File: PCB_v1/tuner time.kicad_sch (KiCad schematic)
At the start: 13 parts, among them U1 C1F 2

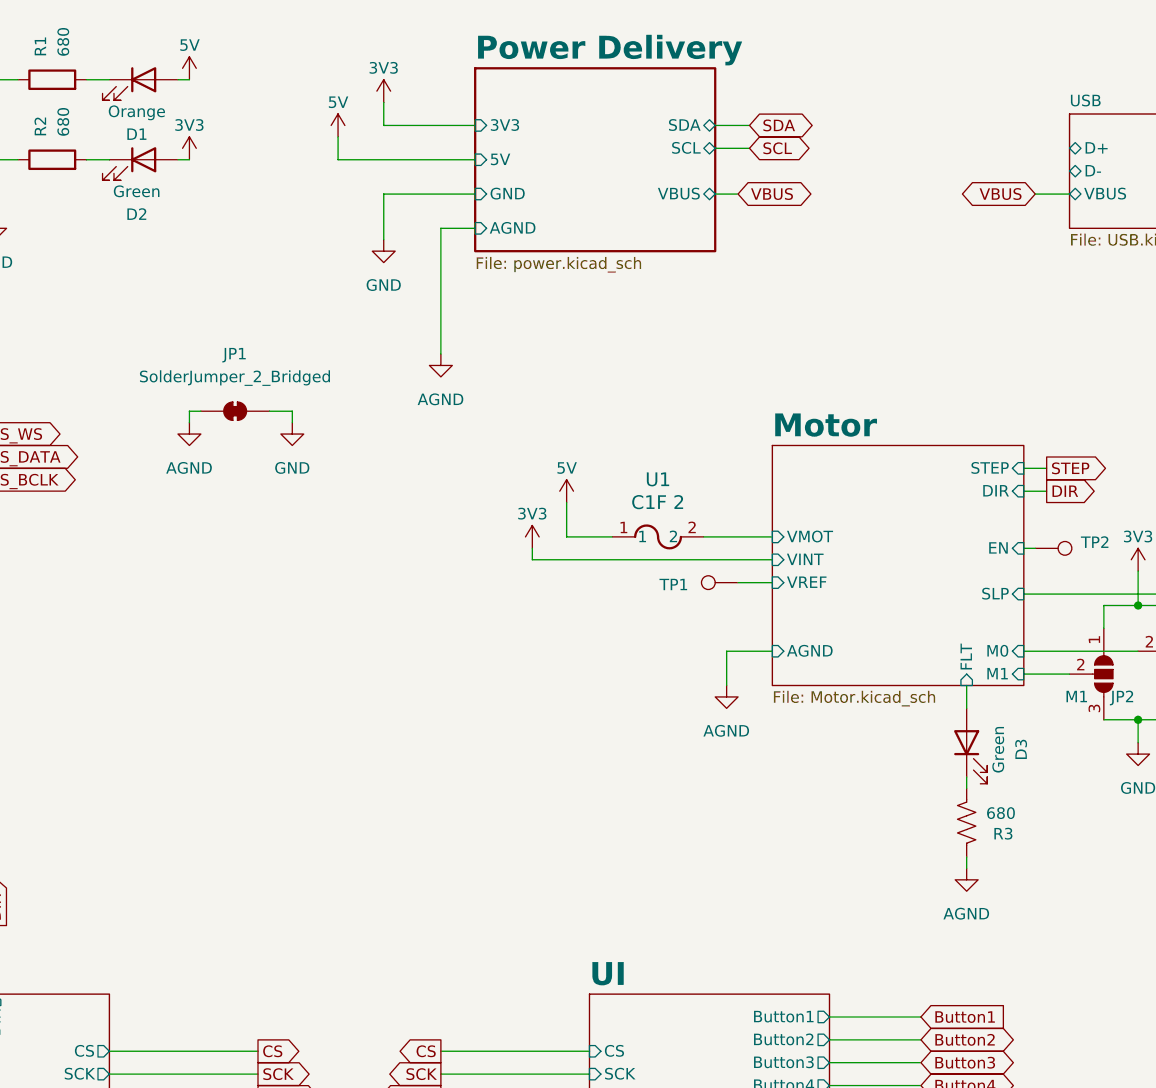
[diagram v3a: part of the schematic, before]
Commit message: Main routes done, no power planes, no DRC
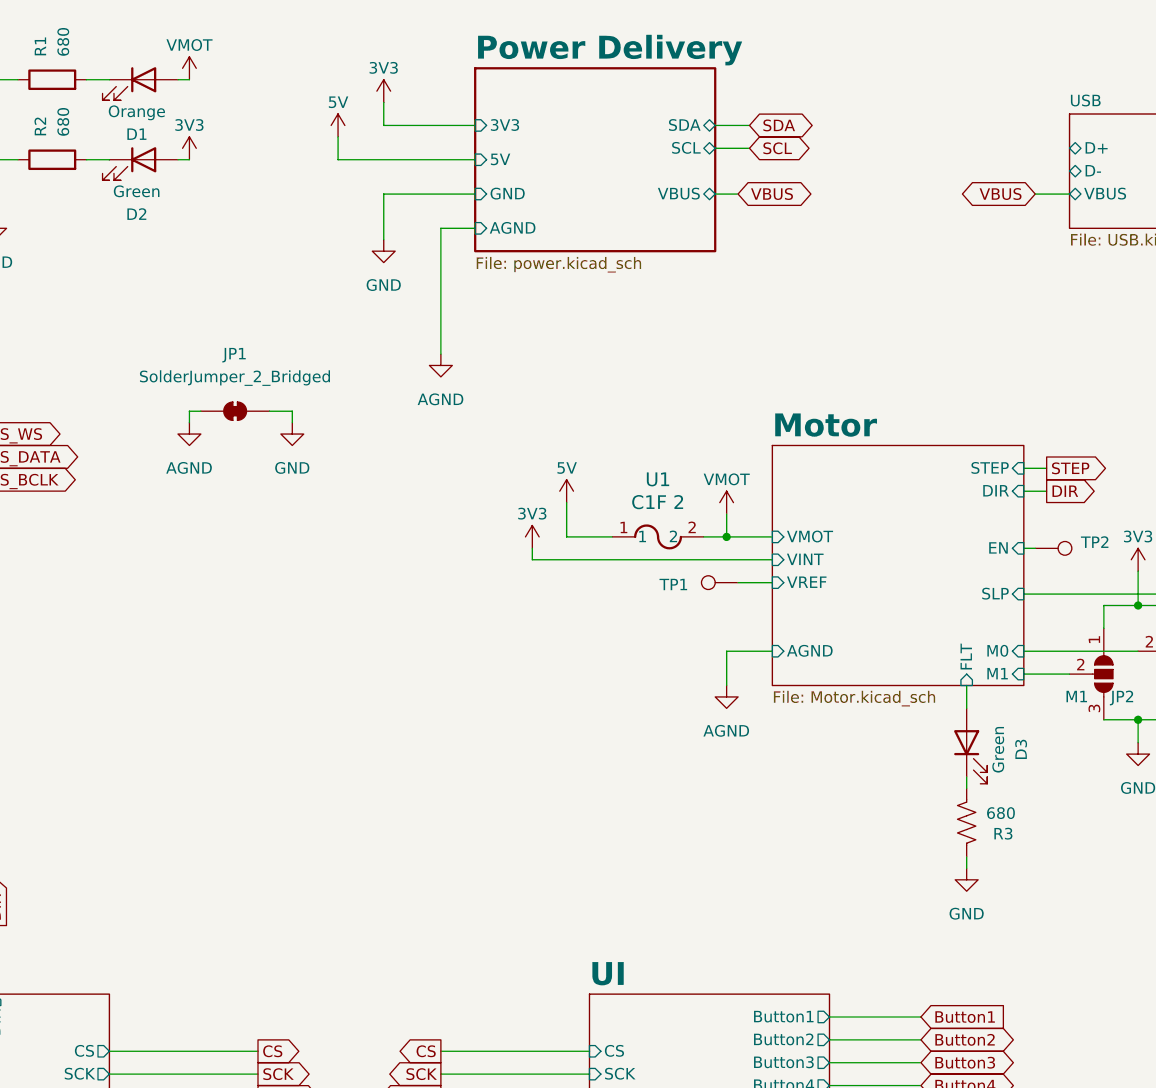
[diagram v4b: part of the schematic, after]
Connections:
- net 5V: no longer D1.2 (A)
- net AGND: no longer R3.2
- net GND: now also R3.2
- net Motor/VMOT renamed VMOT
- net VMOT: now also D1.2 (A)
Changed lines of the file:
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@@
 		(color 0 0 0 0)
 	)
+	(junction
+		(at 198.12 74.93)
+		(diameter 0)
+		(color 0 0 0 0)
+	)
 	(wire
 		(pts
@@
 	(wire
 		(pts
+			(xy 198.12 72.39) (xy 198.12 74.93)
+		)
+		(stroke
+			(width 0)
+			(type default)
+		)
+	)
+	(wire
+		(pts
 			(xy 149.86 60.96) (xy 147.32 60.96)
 		)
@@
 	(wire
 		(pts
+			(xy 198.12 74.93) (xy 203.2 74.93)
+		)
+		(stroke
+			(width 0)
+			(type default)
+		)
+	)
+	(wire
+		(pts
 			(xy 232.41 36.83) (xy 236.22 36.83)
 		)
@@
 	(wire
 		(pts
-			(xy 195.58 74.93) (xy 203.2 74.93)
+			(xy 195.58 74.93) (xy 198.12 74.93)
 		)
 		(stroke
@@
 			)
 		)
-		(property "Value" "AGND"
+		(property "Value" "GND"
 			(at 224.79 116.84 0)
 			(effects
@@
 	)
 	(symbol
-		(lib_id "power:VCC")
-		(at 138.43 24.13 0)
-		(unit 1)
-		(exclude_from_sim no)
-		(in_bom yes)
-		(on_board yes)
-		(dnp no)
-		(property "Reference" "#PWR07"
-			(at 138.43 27.94 0)
-			(effects
-				(font
-					(size 1.27 1.27)
-				)
-				(hide yes)
-			)
-		)
-		(property "Value" "5V"
-			(at 138.43 20.32 0)
-			(effects
-				(font
-					(size 1.27 1.27)
-				)
-			)
-		)
-		(property "Footprint" ""
-			(at 138.43 24.13 0)
-			(effects
-				(font
-					(size 1.27 1.27)
-				)
-				(hide yes)
-			)
-		)
-		(property "Datasheet" ""
-			(at 138.43 24.13 0)
-			(effects
-				(font
-					(size 1.27 1.27)
-				)
-				(hide yes)
-			)
-		)
-		(property "Description" "Power symbol creates a global label with name \"VCC\""
-			(at 138.43 24.13 0)
-			(effects
-				(font
-					(size 1.27 1.27)
-				)
-				(hide yes)
-			)
-		)
-		(pin "1"
-		)
-		(instances
-			(project "tuner time"
-				(path "/353cef6a-fb6e-40d9-89f8-eb54b7aa5118"
-					(reference "#PWR07")
-					(unit 1)
-				)
-			)
-		)
-	)
-	(symbol
 		(lib_id "power:GND")
 		(at 116.84 39.37 0)
@@
 	)
 	(symbol
+		(lib_id "power:VCC")
+		(at 138.43 24.13 0)
+		(unit 1)
+		(exclude_from_sim no)
+		(in_bom yes)
+		(on_board yes)
+		(dnp no)
+		(property "Reference" "#PWR0115"
+			(at 138.43 27.94 0)
+			(effects
+				(font
+					(size 1.27 1.27)
+				)
+				(hide yes)
+			)
+		)
+		(property "Value" "VMOT"
+			(at 138.43 20.32 0)
+			(effects
+				(font
+					(size 1.27 1.27)
+				)
+			)
+		)
+		(property "Footprint" ""
+			(at 138.43 24.13 0)
+			(effects
+				(font
+					(size 1.27 1.27)
+				)
+				(hide yes)
+			)
+		)
+		(property "Datasheet" ""
+			(at 138.43 24.13 0)
+			(effects
+				(font
+					(size 1.27 1.27)
+				)
+				(hide yes)
+			)
+		)
+		(property "Description" "Power symbol creates a global label with name \"VCC\""
+			(at 138.43 24.13 0)
+			(effects
+				(font
+					(size 1.27 1.27)
+				)
+				(hide yes)
+			)
+		)
+		(pin "1"
+		)
+		(instances
+			(project "tuner time"
+				(path "/353cef6a-fb6e-40d9-89f8-eb54b7aa5118"
+					(reference "#PWR0115")
+					(unit 1)
+				)
+			)
+		)
+	)
+	(symbol
 		(lib_id "power:GND")
 		(at 166.37 54.61 0)
@@
 					(unit 1)
 				)
+			)
+		)
+	)
+	(symbol
+		(lib_id "power:VCC")
+		(at 198.12 72.39 0)
+		(unit 1)
+		(exclude_from_sim no)
+		(in_bom yes)
+		(on_board yes)
+		(dnp no)
+		(property "Reference" "#PWR07"
+			(at 198.12 76.2 0)
+			(effects
+				(font
+					(size 1.27 1.27)
+				)
+				(hide yes)
+			)
+		)
+		(property "Value" "VMOT"
+			(at 198.12 68.58 0)
+			(effects
+				(font
+					(size 1.27 1.27)
+				)
+			)
+		)
+		(property "Footprint" ""
+			(at 198.12 72.39 0)
+			(effects
+				(font
+					(size 1.27 1.27)
+				)
+				(hide yes)
+			)
+		)
+		(property "Datasheet" ""
+			(at 198.12 72.39 0)
+			(effects
+				(font
+					(size 1.27 1.27)
+				)
+				(hide yes)
+			)
+		)
+		(property "Description" "Power symbol creates a global label with name \"VCC\""
+			(at 198.12 72.39 0)
+			(effects
+				(font
+					(size 1.27 1.27)
+				)
+				(hide yes)
+			)
+		)
+		(pin "1"
+		)
+		(instances
+			(project "tuner time"
+				(path "/353cef6a-fb6e-40d9-89f8-eb54b7aa5118"
+					(reference "#PWR07")
+					(unit 1)
+				)

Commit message: Power Layout done
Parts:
- added H1, H2: MountingHole, MountingHole:MountingHole_2.2mm_M2_DIN965_Pad_TopOnly, symbol Mechanical:MountingHole
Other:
- sheet MCU ports: added BAT_EMPTY; removed none
- sheet Power Delivery ports: added BAT_EMPTY; removed none
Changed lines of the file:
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@@
 	(wire
 		(pts
+			(xy 199.39 40.64) (xy 196.85 40.64)
+		)
+		(stroke
+			(width 0)
+			(type default)
+		)
+	)
+	(wire
+		(pts
 			(xy 243.84 78.74) (xy 243.84 82.55)
 		)
@@
 	(wire
 		(pts
+			(xy 129.54 152.4) (xy 139.7 152.4)
+		)
+		(stroke
+			(width 0)
+			(type default)
+		)
+	)
+	(wire
+		(pts
 			(xy 209.55 138.43) (xy 219.71 138.43)
 		)
@@
 		)
 	)
+	(global_label "BAT_EMPTY"
+		(shape input)
+		(at 139.7 152.4 0)
+		(fields_autoplaced yes)
+		(effects
+			(font
+				(size 1.27 1.27)
+			)
+			(justify left)
+		)
+		(property "Intersheetrefs" "${INTERSHEET_REFS}"
+			(at 152.9056 152.4 0)
+			(effects
+				(font
+					(size 1.27 1.27)
+				)
+				(justify left)
+				(hide yes)
+			)
+		)
+	)
 	(global_label "SCK"
 		(shape output)
@@
 		)
 	)
+	(global_label "BAT_EMPTY"
+		(shape input)
+		(at 199.39 40.64 0)
+		(fields_autoplaced yes)
+		(effects
+			(font
+				(size 1.27 1.27)
+			)
+			(justify left)
+		)
+		(property "Intersheetrefs" "${INTERSHEET_REFS}"
+			(at 212.5956 40.64 0)
+			(effects
+				(font
+					(size 1.27 1.27)
+				)
+				(justify left)
+				(hide yes)
+			)
+		)
+	)
 	(global_label "MOSI"
 		(shape output)
@@
 	)
 	(symbol
+		(lib_id "Mechanical:MountingHole")
+		(at 19.05 17.78 0)
+		(unit 1)
+		(exclude_from_sim yes)
+		(in_bom no)
+		(on_board yes)
+		(dnp no)
+		(fields_autoplaced yes)
+		(property "Reference" "H1"
+			(at 21.59 16.5099 0)
+			(effects
+				(font
+					(size 1.27 1.27)
+				)
+				(justify left)
+			)
+		)
+		(property "Value" "MountingHole"
+			(at 21.59 19.0499 0)
+			(effects
+				(font
+					(size 1.27 1.27)
+				)
+				(justify left)
+			)
+		)
+		(property "Footprint" "MountingHole:MountingHole_2.2mm_M2_DIN965_Pad_TopOnly"
+			(at 19.05 17.78 0)
+			(effects
+				(font
+					(size 1.27 1.27)
+				)
+				(hide yes)
+			)
+		)
+		(property "Datasheet" "~"
+			(at 19.05 17.78 0)
+			(effects
+				(font
+					(size 1.27 1.27)
+				)
+				(hide yes)
+			)
+		)
+		(property "Description" "Mounting Hole without connection"
+			(at 19.05 17.78 0)
+			(effects
+				(font
+					(size 1.27 1.27)
+				)
+				(hide yes)
+			)
+		)
+		(instances
+			(project ""
+				(path "/353cef6a-fb6e-40d9-89f8-eb54b7aa5118"
+					(reference "H1")
+					(unit 1)
+				)
+			)
+		)
+	)
+	(symbol
 		(lib_id "power:VCC")
 		(at 180.34 71.12 0)
@@
 	)
 	(symbol
+		(lib_id "Mechanical:MountingHole")
+		(at 19.05 24.13 0)
+		(unit 1)
+		(exclude_from_sim yes)
+		(in_bom no)
+		(on_board yes)
+		(dnp no)
+		(fields_autoplaced yes)
+		(property "Reference" "H2"
+			(at 21.59 22.8599 0)
+			(effects
+				(font
+					(size 1.27 1.27)
+				)
+				(justify left)
+			)
+		)
+		(property "Value" "MountingHole"
+			(at 21.59 25.3999 0)
+			(effects
+				(font
+					(size 1.27 1.27)
+				)
+				(justify left)
+			)
+		)
+		(property "Footprint" "MountingHole:MountingHole_2.2mm_M2_DIN965_Pad_TopOnly"
+			(at 19.05 24.13 0)
+			(effects
+				(font
+					(size 1.27 1.27)
+				)
+				(hide yes)
+			)
+		)
+		(property "Datasheet" "~"
+			(at 19.05 24.13 0)
+			(effects
+				(font
+					(size 1.27 1.27)
+				)
+				(hide yes)
+			)
+		)
+		(property "Description" "Mounting Hole without connection"
+			(at 19.05 24.13 0)
+			(effects
+				(font
+					(size 1.27 1.27)
+				)
+				(hide yes)
+			)
+		)
+		(instances
+			(project "tuner time"
+				(path "/353cef6a-fb6e-40d9-89f8-eb54b7aa5118"
+					(reference "H2")
+					(unit 1)
+				)
+			)
+		)
+	)
+	(symbol
 		(lib_id "power:GND")
 		(at 254 87.63 0)
@@
 			)
 		)
+		(pin "BAT_EMPTY" output
+			(at 196.85 40.64 0)
+			(effects
+				(font
+					(size 1.27 1.27)
+				)
+				(justify right)
+			)
+		)
 		(instances
 			(project "tuner time"
@@
 			)
 		)
+		(pin "BAT_EMPTY" input
+			(at 129.54 152.4 0)
+			(effects
+				(font
+					(size 1.27 1.27)
+				)
+				(justify right)
+			)
+		)

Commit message: before annonation reset
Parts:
- F2: renamed from U1; MFP (none) -> 5923-C1F2TR-ND
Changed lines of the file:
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@@
 		(dnp no)
 		(fields_autoplaced yes)
-		(property "Reference" "U1"
+		(property "Reference" "F2"
 			(at 190.5 68.58 0)
 			(effects
@@
 			)
 		)
-		(property "MFP" ""
+		(property "MFP" "5923-C1F2TR-ND"
 			(at 185.42 74.93 0)
 			(effects
@@
 			(project ""
 				(path "/353cef6a-fb6e-40d9-89f8-eb54b7aa5118"
-					(reference "U1")
+					(reference "F2")
 					(unit 1)
 				)

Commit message: pushing BOM
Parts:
- F1: renamed from F2; MFP 5923-C1F2TR-ND -> C1F 2 (CA0612KRX7R7BB104)
- H1, H2, JP1, JP2, JP3, JP4, TP1, TP2: MFP (none) -> N/A
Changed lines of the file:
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@@
 		(dnp no)
 		(fields_autoplaced yes)
-		(property "Reference" "F2"
+		(property "Reference" "F1"
 			(at 190.5 68.58 0)
 			(effects
@@
 			)
 		)
-		(property "Datasheet" "C1F 2"
+		(property "Datasheet" ""
 			(at 185.42 74.93 0)
 			(effects
@@
 			)
 		)
-		(property "MFP" "5923-C1F2TR-ND"
+		(property "MFP" "C1F 2 (CA0612KRX7R7BB104)"
 			(at 185.42 74.93 0)
 			(effects
@@
 			(project ""
 				(path "/353cef6a-fb6e-40d9-89f8-eb54b7aa5118"
-					(reference "F2")
+					(reference "F1")
 					(unit 1)
 				)
@@
 			)
 		)
+		(property "MFP" "N/A"
+			(at 143.51 60.96 0)
+			(effects
+				(font
+					(size 1.27 1.27)
+				)
+				(hide yes)
+			)
+		)
 		(pin "2"
 		)
@@
 			)
 		)
-		(property "MFP" ""
+		(property "MFP" "N/A"
 			(at 232.41 76.2 0)
 			(effects
@@
 			)
 		)
-		(property "MFP" ""
+		(property "MFP" "N/A "
 			(at 240.03 90.17 0)
 			(effects
@@
 		(dnp no)
 		(fields_autoplaced yes)
-		(property "Reference" "#PWR020"
+		(property "Reference" "#PWR021"
 			(at 224.79 118.11 0)
 			(effects
@@
 			(project "tuner time"
 				(path "/353cef6a-fb6e-40d9-89f8-eb54b7aa5118"
-					(reference "#PWR020")
+					(reference "#PWR021")
 					(unit 1)
 				)
@@
 		(dnp no)
 		(fields_autoplaced yes)
-		(property "Reference" "#PWR018"
+		(property "Reference" "#PWR019"
 			(at 214.63 161.29 0)
 			(effects
@@
 			(project "tuner time"
 				(path "/353cef6a-fb6e-40d9-89f8-eb54b7aa5118"
-					(reference "#PWR018")
+					(reference "#PWR019")
 					(unit 1)
 				)
@@
 			)
 		)
-		(property "MFP" ""
+		(property "MFP" "N/A "
 			(at 247.65 87.63 0)
 			(effects
@@
 			)
 		)
+		(property "MFP" "N/A"
+			(at 19.05 17.78 0)
+			(effects
+				(font
+					(size 1.27 1.27)
+				)
+				(hide yes)
+			)
+		)
 		(instances
 			(project ""
@@
 		(dnp no)
 		(fields_autoplaced yes)
-		(property "Reference" "#PWR025"
+		(property "Reference" "#PWR026"
 			(at 267.97 45.72 0)
 			(effects
@@
 			(project "tuner time"
 				(path "/353cef6a-fb6e-40d9-89f8-eb54b7aa5118"
-					(reference "#PWR025")
+					(reference "#PWR026")
 					(unit 1)
 				)
@@
 			)
 		)
-		(property "MFP" ""
+		(property "MFP" "N/A "
 			(at 254 81.28 0)
 			(effects
@@
 		(on_board yes)
 		(dnp no)
-		(property "Reference" "#PWR021"
+		(property "Reference" "#PWR022"
 			(at 243.84 82.55 0)
 			(effects
@@
 			(project "tuner time"
 				(path "/353cef6a-fb6e-40d9-89f8-eb54b7aa5118"
-					(reference "#PWR021")
+					(reference "#PWR022")
 					(unit 1)
 				)
@@
 		(on_board yes)
 		(dnp no)
-		(property "Reference" "#PWR019"
+		(property "Reference" "#PWR020"
 			(at 214.63 146.05 0)
 			(effects
@@
 			(project "tuner time"
 				(path "/353cef6a-fb6e-40d9-89f8-eb54b7aa5118"
-					(reference "#PWR019")
+					(reference "#PWR020")
 					(unit 1)
 				)
@@
 			)
 		)
+		(property "MFP" "N/A"
+			(at 19.05 24.13 0)
+			(effects
+				(font
+					(size 1.27 1.27)
+				)
+				(hide yes)
+			)
+		)
 		(instances
 			(project "tuner time"
@@
 		(dnp no)
 		(fields_autoplaced yes)
-		(property "Reference" "#PWR024"
+		(property "Reference" "#PWR025"
 			(at 254 93.98 0)
 			(effects
@@
 			(project "tuner time"
 				(path "/353cef6a-fb6e-40d9-89f8-eb54b7aa5118"
-					(reference "#PWR024")
+					(reference "#PWR025")
 					(unit 1)
 				)
@@
 		(dnp no)
 		(fields_autoplaced yes)
-		(property "Reference" "#PWR017"
+		(property "Reference" "#PWR018"
 			(at 198.12 97.79 0)
 			(effects
@@
 			(project "tuner time"
 				(path "/353cef6a-fb6e-40d9-89f8-eb54b7aa5118"
-					(reference "#PWR017")
+					(reference "#PWR018")
 					(unit 1)
 				)
@@
 		(on_board yes)
 		(dnp no)
-		(property "Reference" "#PWR0115"
+		(property "Reference" "#PWR07"
 			(at 138.43 27.94 0)
 			(effects
@@
 			(project "tuner time"
 				(path "/353cef6a-fb6e-40d9-89f8-eb54b7aa5118"
-					(reference "#PWR0115")
+					(reference "#PWR07")
 					(unit 1)
 				)
@@
 		(on_board yes)
 		(dnp no)
-		(property "Reference" "#PWR023"
+		(property "Reference" "#PWR024"
 			(at 254 78.74 0)
 			(effects
@@
 			(project "tuner time"
 				(path "/353cef6a-fb6e-40d9-89f8-eb54b7aa5118"
-					(reference "#PWR023")
+					(reference "#PWR024")
 					(unit 1)
 				)
@@
 			)
 		)
-		(property "MFP" ""
+		(property "MFP" "N/A"
 			(at 199.39 80.01 0)
 			(effects
@@
 		(dnp no)
 		(fields_autoplaced yes)
-		(property "Reference" "#PWR022"
+		(property "Reference" "#PWR023"
 			(at 243.84 104.14 0)
 			(effects
@@
 			(project "tuner time"
 				(path "/353cef6a-fb6e-40d9-89f8-eb54b7aa5118"
-					(reference "#PWR022")
+					(reference "#PWR023")
 					(unit 1)
 				)
@@
 		(on_board yes)
 		(dnp no)
-		(property "Reference" "#PWR07"
+		(property "Reference" "#PWR017"
 			(at 198.12 76.2 0)
 			(effects
@@
 			(project "tuner time"
 				(path "/353cef6a-fb6e-40d9-89f8-eb54b7aa5118"
-					(reference "#PWR07")
-					(unit 1)
-				)
+					(reference "#PWR017")
+					(unit 1)
+				)
